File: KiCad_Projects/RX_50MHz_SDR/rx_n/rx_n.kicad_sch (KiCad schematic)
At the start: 0 parts

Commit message: Add Murata 10.7MHz IF filter technical reference
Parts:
- added U1: LT5560, Package_DFN_QFN:DFN-8-1EP_3x3mm_P0.5mm_EP1.66x2.38mm, symbol RF_Mixer:LT5560
- added U2: AP2112K-3.3, Package_TO_SOT_SMD:SOT-23-5, symbol Regulator_Linear:AP2112K-3.3
- added U3: ESP32-S3, Package_DFN_QFN:QFN-56-1EP_7x7mm_P0.4mm_EP4x4mm, symbol MCU_Espressif:ESP32-S3
- added Y1: Si5351A-B-GT, Package_SO:MSOP-10_3x3mm_P0.5mm, symbol Oscillator:Si5351A-B-GT
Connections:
- new net: U3.2 (VDD3P3), U3.3 (VDD3P3)
- new net: U3.55 (VDDA), U3.56 (VDDA)

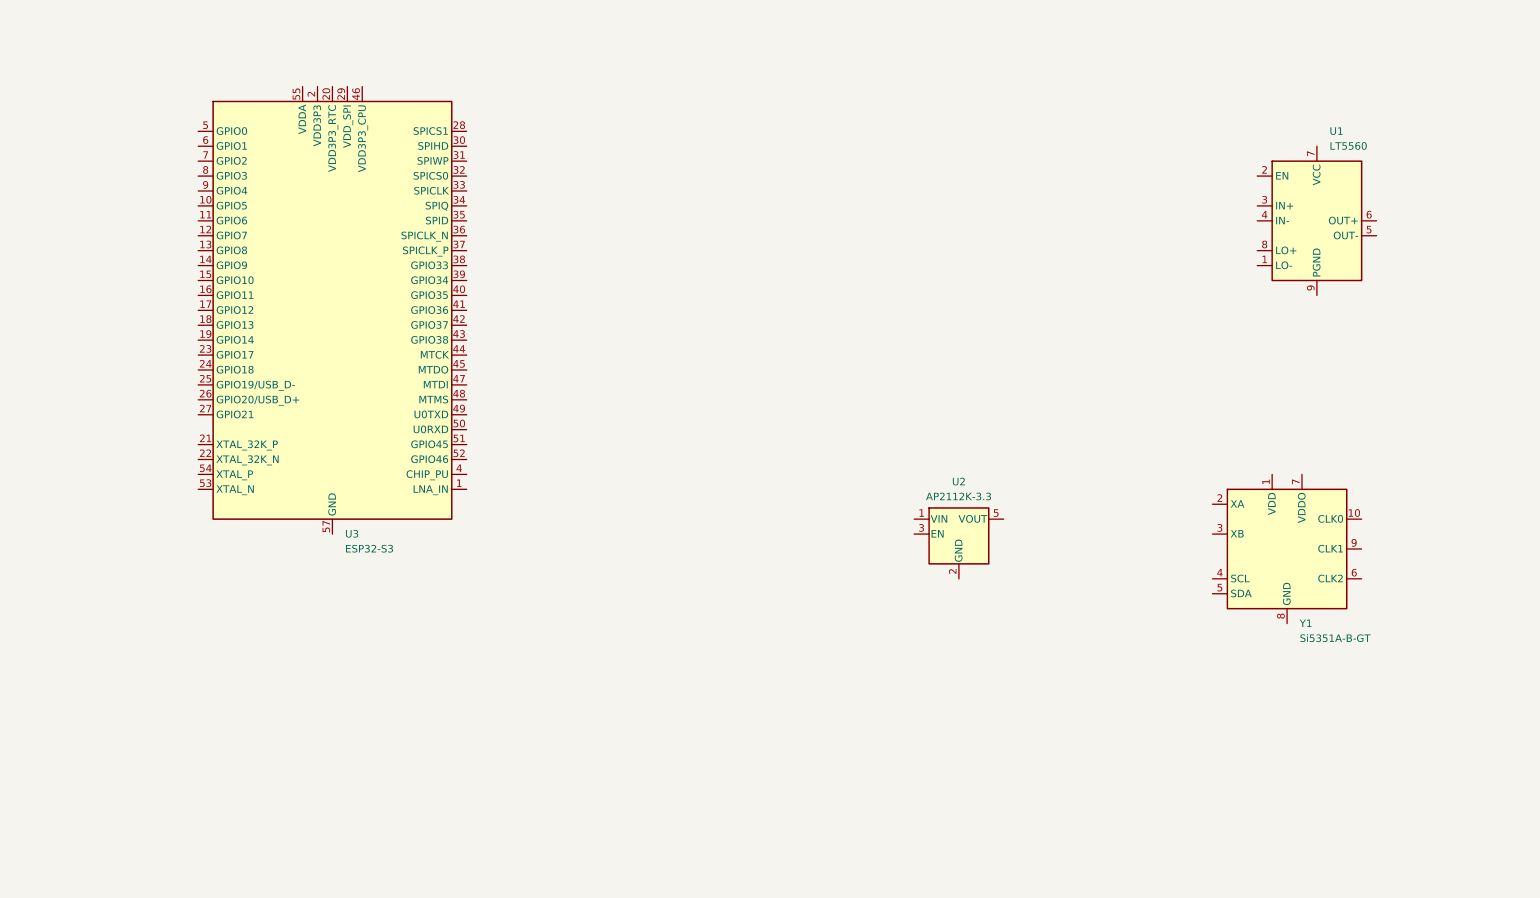
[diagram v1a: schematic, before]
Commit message: Update IF filter reference with footprint details and add KiCad library files
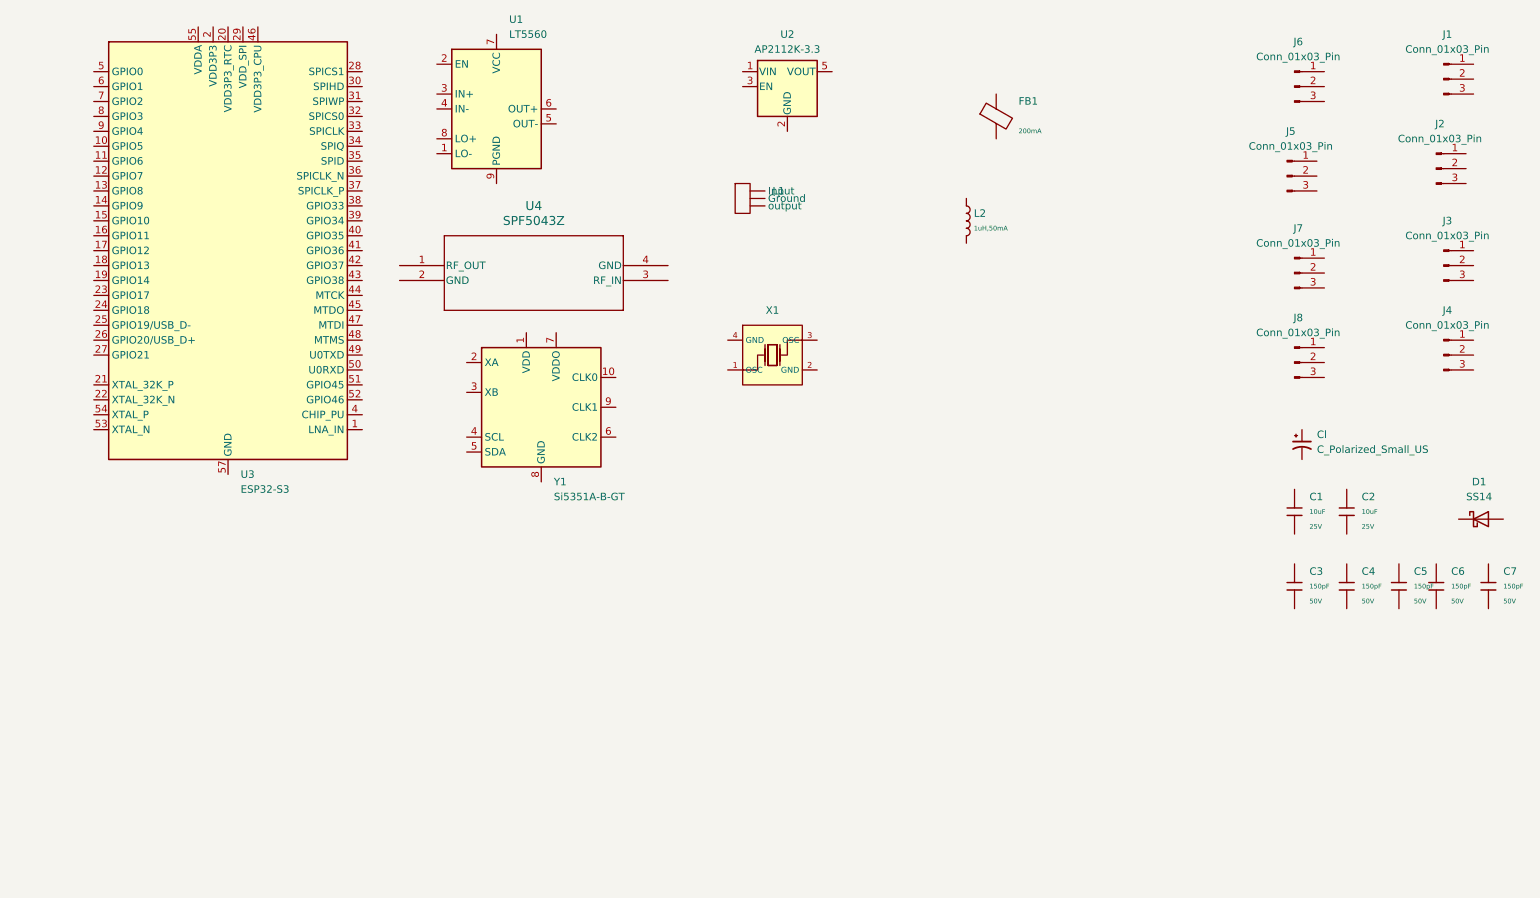
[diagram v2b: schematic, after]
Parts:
- added C1, C2: 10uF, PCM_JLCPCB:C_0805, symbol PCM_JLCPCB-Capacitors:0805,10uF
- added C3, C4, C5, C6, C7: 150pF, PCM_JLCPCB:C_0603, symbol PCM_JLCPCB-Capacitors:0603,150pF
- added Cl: C_Polarized_Small_US, symbol Device:C_Polarized_Small_US
- added D1: SS14, Diode_SMD:D_SMA, symbol Diode:SS14
- added FB1: ~, PCM_JLCPCB:FB_0603, symbol PCM_JLCPCB-Inductors:Ferrite,0603
- added J1, J2, J3, J4, J5, J6, J7, J8: Conn_01x03_Pin, symbol Connector:Conn_01x03_Pin
- added L1: ~, symbol radio:IF Filter 230kHz
- added L2: 1uH,50mA, PCM_JLCPCB:L_0805, symbol PCM_JLCPCB-Inductors:1uH,50mA
- added U4: SPF5043Z, SPF5043Z_QOR, symbol radio:SPF5043Z
- added X1: X322516MLB4SI, PCM_JLCPCB:OSC-SMD_4P-L3.2-W2.5-BL, symbol PCM_JLCPCB-Crystals:Crystal, 16MHz, 9pF
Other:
- moved on the sheet: U1, U2, U3, Y1

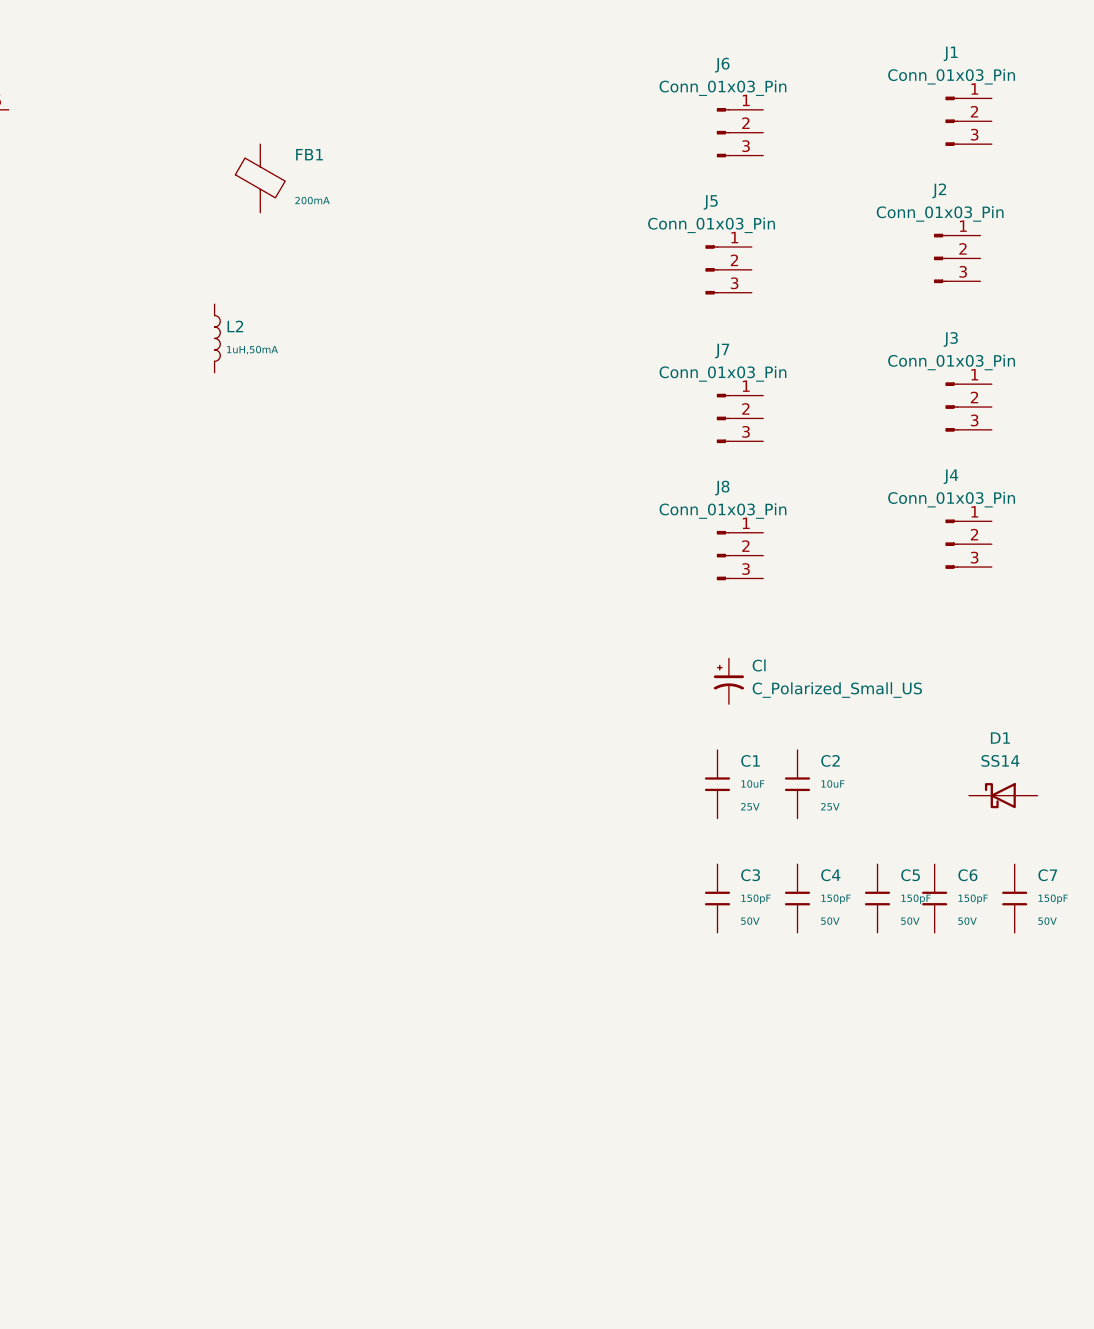
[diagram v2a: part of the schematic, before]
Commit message: Add BGS12PL6 RF switch and INA219 current sensor to Kraft6M KiCad library
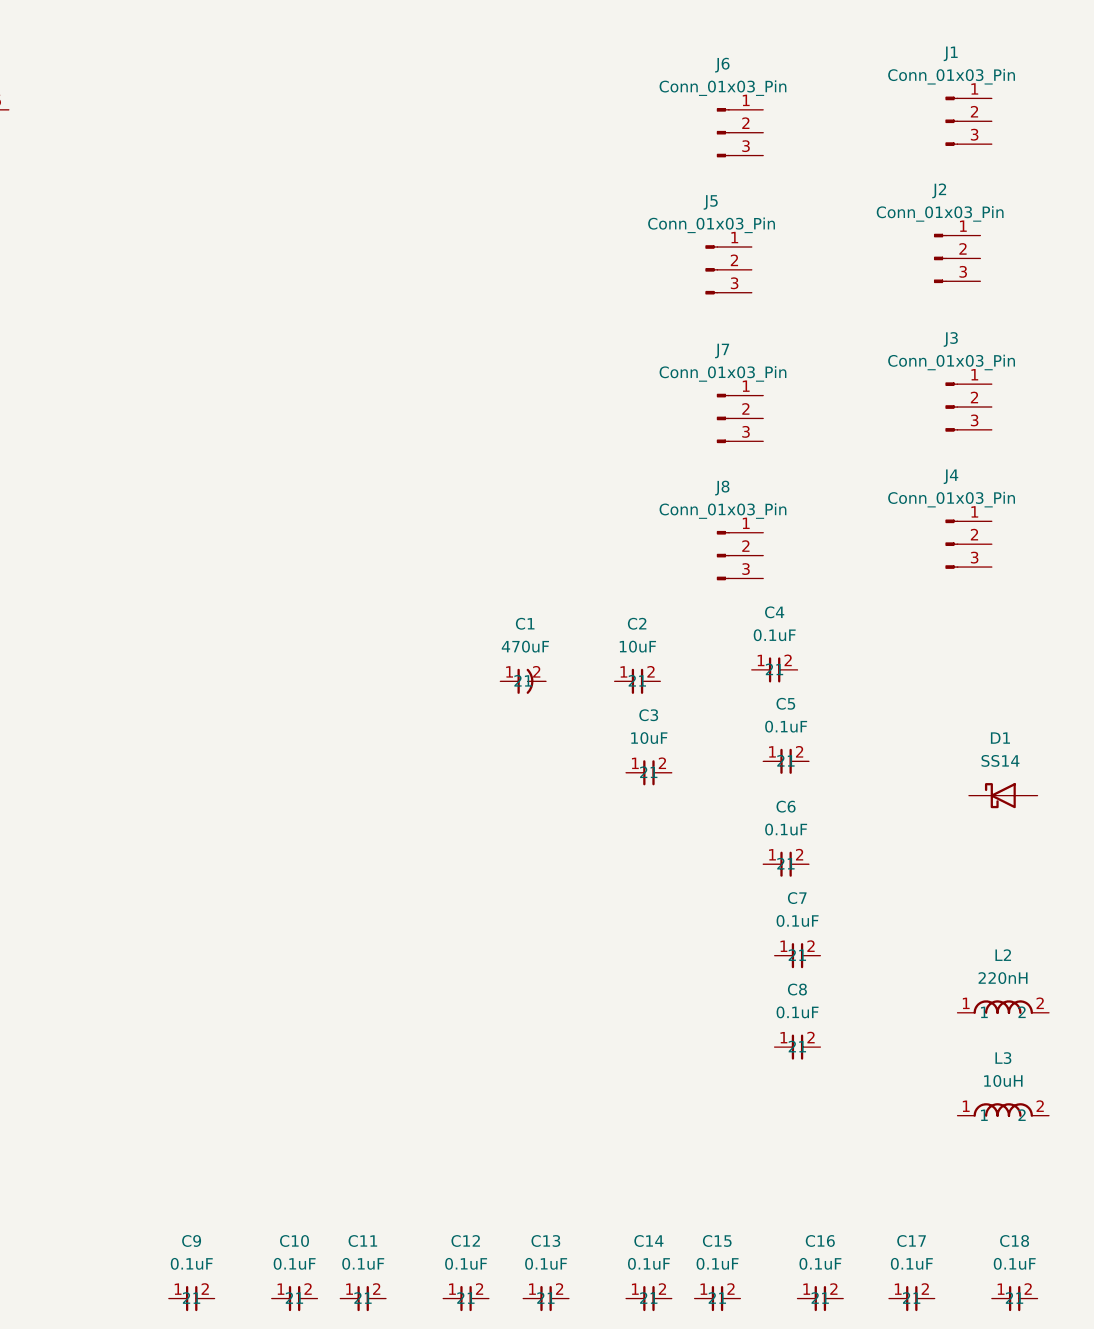
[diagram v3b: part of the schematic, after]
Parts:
- removed C1, C2: 10uF, PCM_JLCPCB:C_0805, symbol PCM_JLCPCB-Capacitors:0805,10uF
- removed C3, C4, C5, C6, C7: 150pF, PCM_JLCPCB:C_0603, symbol PCM_JLCPCB-Capacitors:0603,150pF
- removed Cl: C_Polarized_Small_US, symbol Device:C_Polarized_Small_US
- removed FB1: ~, PCM_JLCPCB:FB_0603, symbol PCM_JLCPCB-Inductors:Ferrite,0603
- removed L2: 1uH,50mA, PCM_JLCPCB:L_0805, symbol PCM_JLCPCB-Inductors:1uH,50mA
- added C1: 470uF, Capacitor_THT:CP_Radial_D8.0mm_P3.50mm, symbol Kraft6M:C_470uF_Radial
- added C10, C11, C12, C13, C14, C15, C16, C17, C18, C4, C5, C6, C7, C8, C9: 0.1uF, Capacitor_SMD:C_0603_1608Metric, symbol Kraft6M:C_0.1uF_0603
- added C2, C3: 10uF, Capacitor_SMD:C_0805_2012Metric, symbol Kraft6M:C_10uF_0805
- added L2: 220nH, Inductor_SMD:L_0603_1608Metric, symbol Kraft6M:L_220nH_0603
- added L3: 10uH, Inductor_SMD:L_0805_2012Metric, symbol Kraft6M:L_10uH_0805

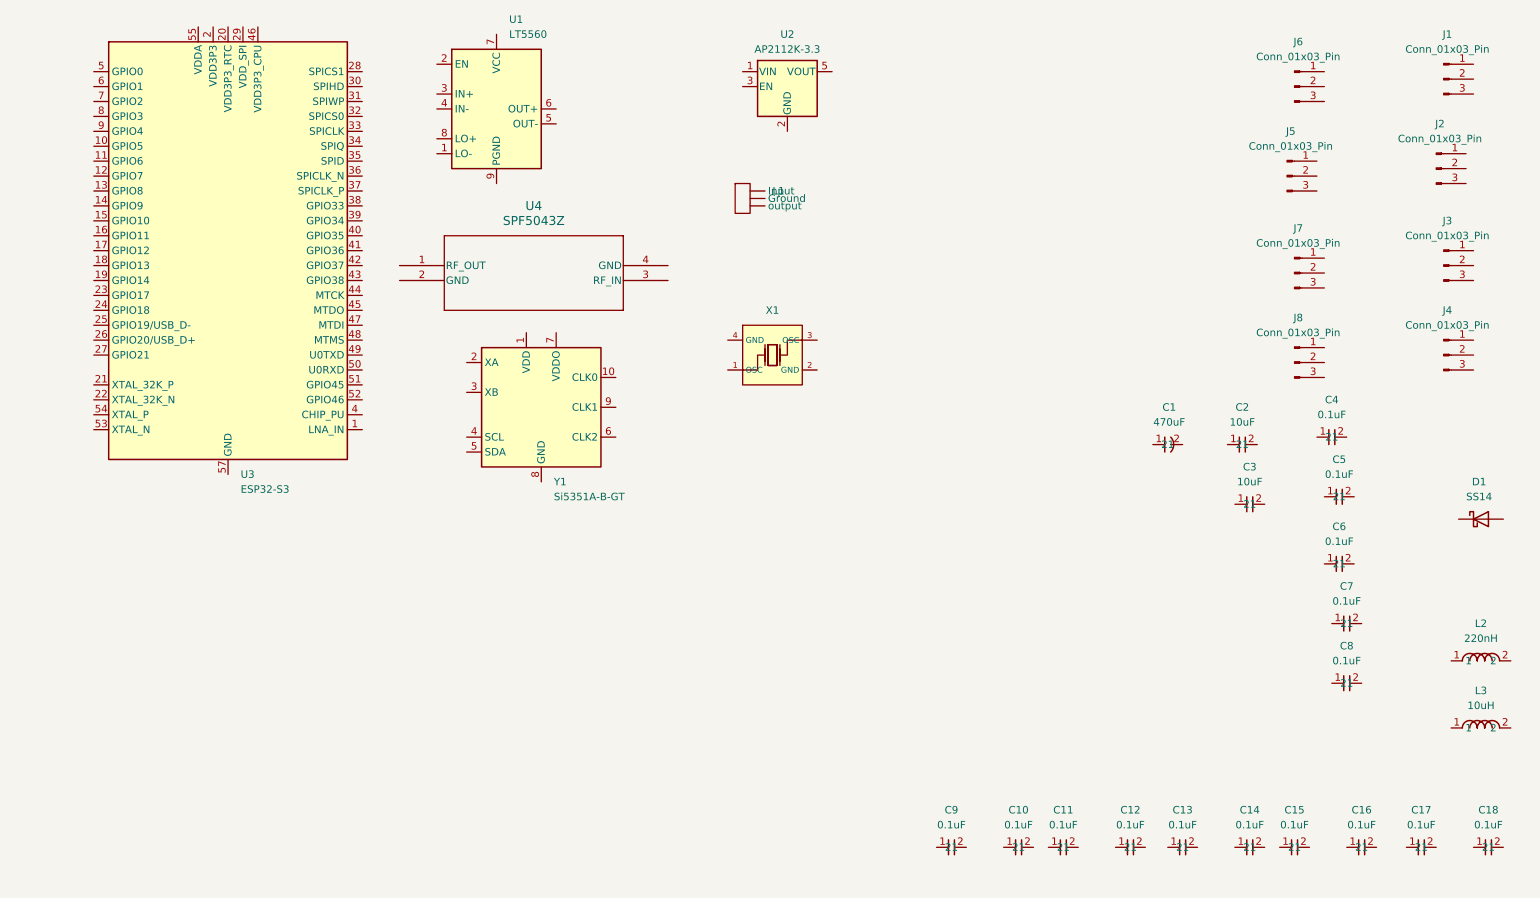
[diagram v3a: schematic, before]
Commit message: Inject missing telemetry components into TX and RX schematic sheets
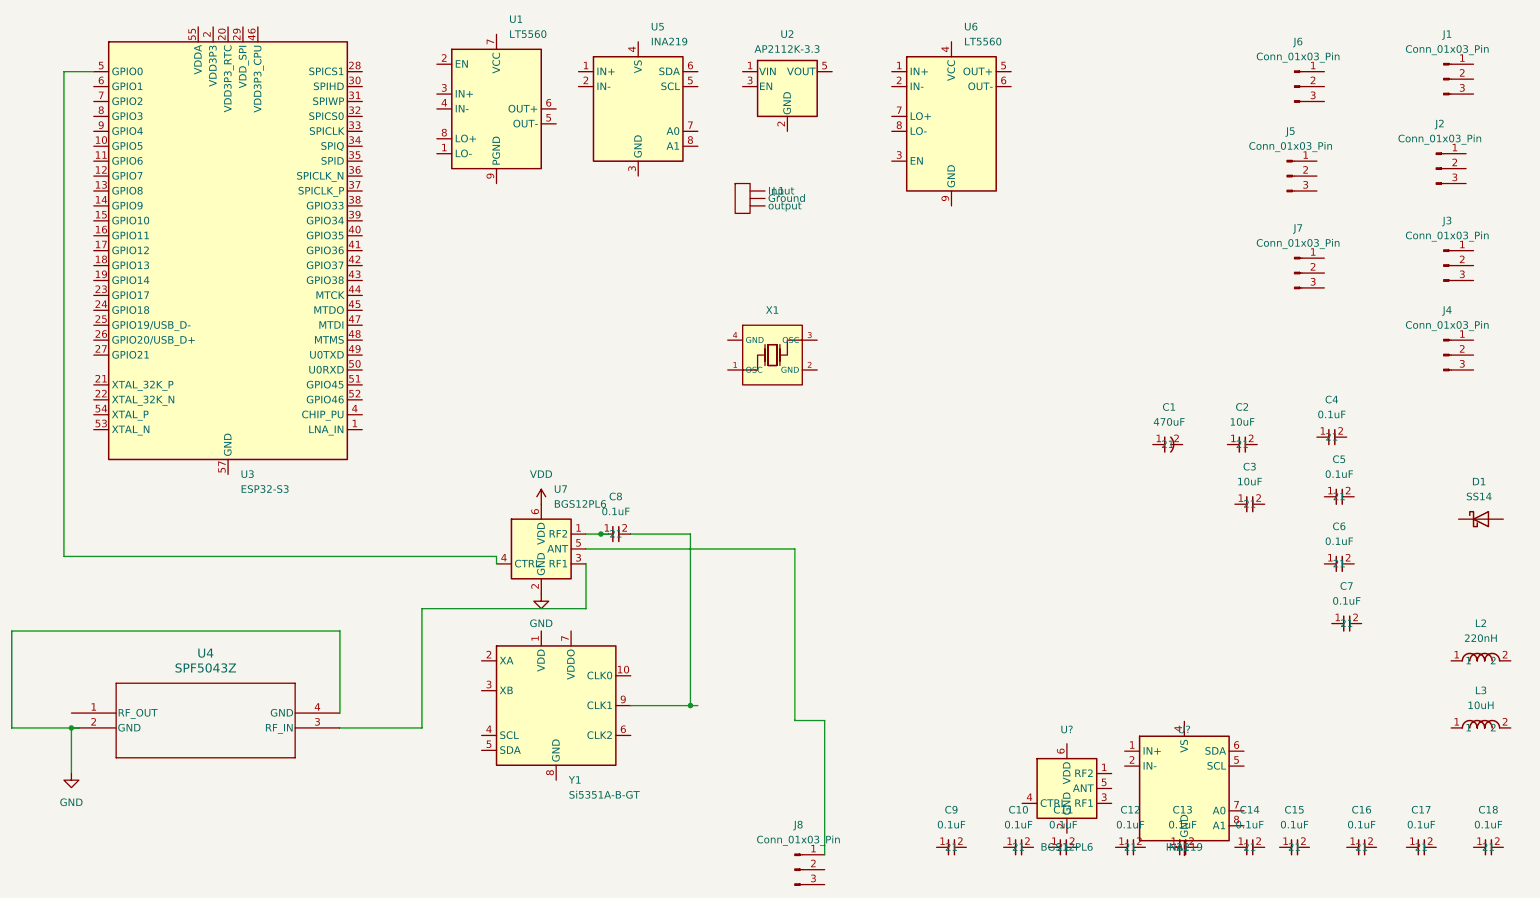
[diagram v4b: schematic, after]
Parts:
- added U5: INA219, Package_TO_SOT_SMD:SOT-23-8, symbol Kraft6M:INA219
- added U6: LT5560, Package_SON:DFN-8-1EP_2x2mm_P0.5mm_EP0.6x1.0mm, symbol Kraft6M:LT5560
- added U7: BGS12PL6, Package_SON:TSLP-6-4_0.7x1.1mm_P0.4mm, symbol Kraft6M:BGS12PL6
- added U?: BGS12PL6, symbol Kraft6M:BGS12PL6
- added U?: INA219, symbol Kraft6M:INA219
- L1: value ~ -> (none)
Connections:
- net at Y1.9 (CLK1): now also C8.2
- net at J8.1 (Pin_1): now also U7.5 (ANT)
- net at C8.1: now also U7.1 (RF2)
- net at U3.5 (GPIO0): now also U7.4 (CTRL)
- net GND: now reaches U4.2 (GND)
- net GND: now also U4.4 (GND), U7.2 (GND)
- net at U4.3 (RF_IN): now also U7.3 (RF1)
- new net VDD: U7.6 (VDD)
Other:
- moved on the sheet: C8, J8, U4, Y1
